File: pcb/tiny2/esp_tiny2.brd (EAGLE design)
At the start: 45 x 95 mm, 35 parts, among them IC1 4000D, Q1 BUZ11BH

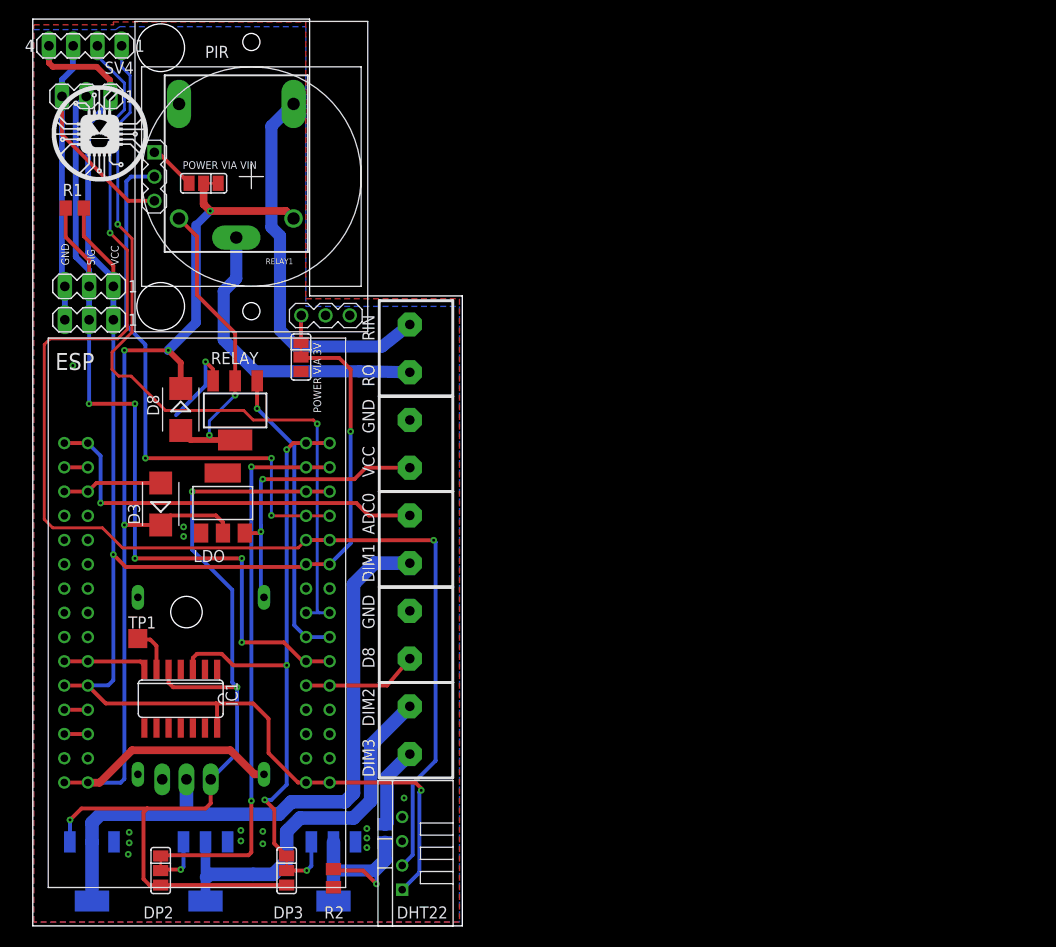
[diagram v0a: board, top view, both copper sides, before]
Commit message: Removed all temp file
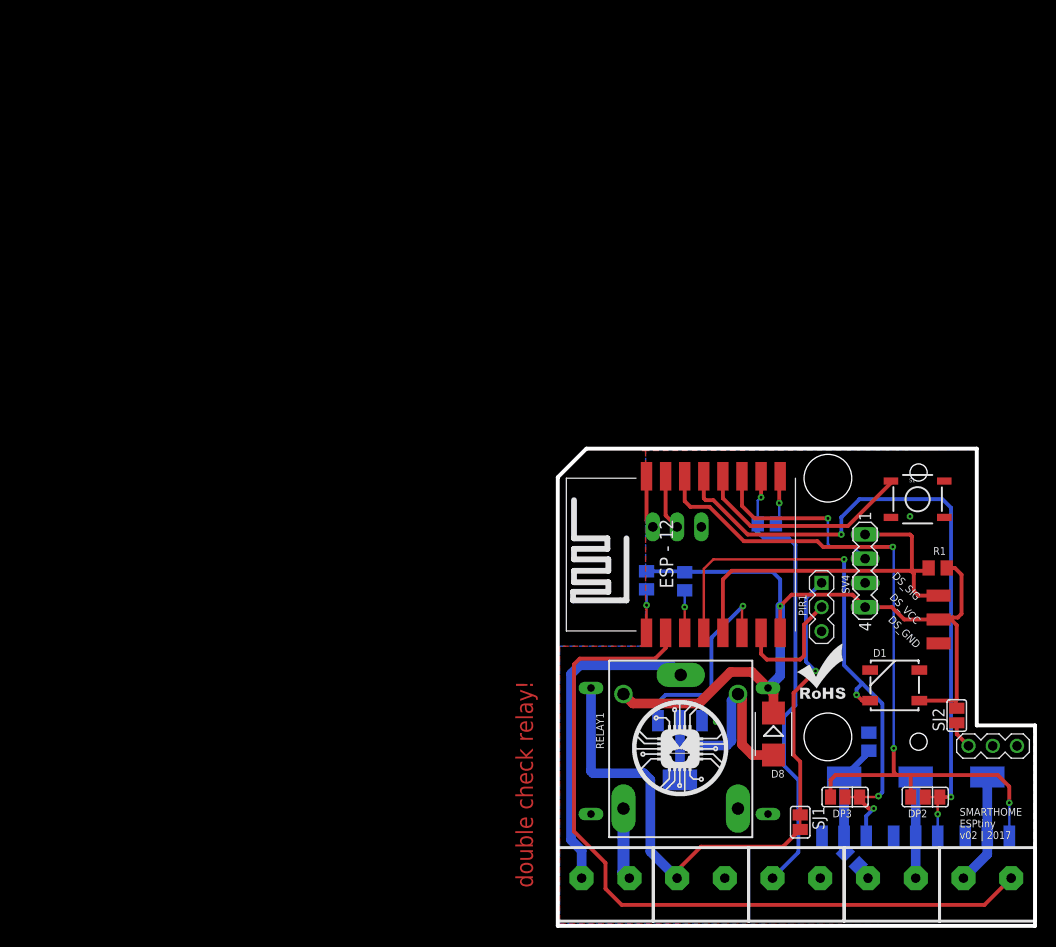
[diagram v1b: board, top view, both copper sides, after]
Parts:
- removed D3: ES2D, diode:SMB
- removed DHT22: TEMP-HUM-SENSOR-DHT22, diy-modules:TEMP-HUM-SENSOR-DHT22
- removed ESP: ESP12E_DEVKIT, ESP12E_DEVKIT:ESP12E_DEVKIT
- removed IC1: 4000D, 40xx:SO14
- removed LDO: REG1117, burr-brown:SOT223
- removed PIR: MOTION-PIR-DYP-ME003, diy-modules:MOTION-PIR-DYP-ME003
- removed Q1: BUZ11BH, transistor-power:TO220BH
- removed SV2, SV3: (no value), con-lstb:MA03-1
- removed TP1: TPTP20SQ, testpad:TP20SQ
- removed U$5, U$6: SMD_SJ_3WAY_CLOSED, JKW_CHIP:SMD_SJ_3WAY_CLOSED
- added D1: (no value), SparkFun-LED:WS2812B
- added DS_GND, DS_SIG, DS_VCC: (no value), wirepad:SMD1,27-2,54
- added PIR1: MOTION-PIR-DYP-ME003, diy-modules:MOTION-PIR-DYP-ME003_FRAMELESS
- added R4, R5, R6: 10k, rcl:M0805
- added S1: TAC_SWITCHSMD, SparkFun-Retired:TACTILE-SWITCH-SMD
- added SJ1: (no value), JKW_CHIP:SMD_SJ_2WAY_CLOSED
- added SJ2: (no value), JKW_CHIP:SMD_SJ_2WAY_OPEN
- added U1: (no value), esp8266modules:ESP12-SMD
- U$12: value MP1584EN_FRAMELESS -> MP1584EN; device JKW_CHIP:MP1584EN_FRAMELESS -> JKW_CHIP:MP1584EN
- moved U$4 104.6 mm to (96.2, 22.7)
- moved SV4 98.5 mm to (87.2, 37.2), turned to 270 degrees
- moved R1 97.9 mm to (94.8, 37.5)
- moved T_DIM1 94.0 mm to (100.0, 12.5), turned to 0 degrees
- moved U$11 88.6 mm to (62.8, 13.6)
- moved U$9 85.8 mm to (79.6, 23.7), flipped to the top
- moved DP2 80.5 mm to (93.5, 13.5), turned to 180 degrees
- moved SV1 76.6 mm to (67.5, 41.8), flipped to the bottom, turned to 0 degrees
- moved RELAY1 76.6 mm to (68.0, 18.9), turned to 270 degrees
- moved T_DIM2 74.7 mm to (92.5, 12.5), turned to 0 degrees
- moved D8 70.8 mm to (77.6, 20.1)
- moved U$3 70.0 mm to (100.0, 4.50), turned to 0 degrees
- moved U$1 61.5 mm to (80.7, 28.9)
- moved U$8 59.5 mm to (60.0, 4.50), turned to 0 degrees
- moved DP3 59.0 mm to (85.1, 13.5), turned to 180 degrees
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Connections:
- removed net DIMM2: DP2.1, ESP.D1, ESP.D11
- removed net N$12: ESP.EN, ESP.EN1
- removed net N$13: ESP.RST, ESP.RST1
- removed net N$14: D3.A, ESP.RSV@1, ESP.RSV@11
- removed net N$17: LDO.3, U$12.VIN, U$7.P$1
- removed net N$24: PIR.4, U$5.1
- removed net N$31: PIR.1, U$6.3
- removed net ONEWIRE_DS12B20: ESP.D7, ESP.D71, R1.1, SV1.2, SV2.2, SV3.2
- removed net RERLAY: ESP.D6, ESP.D61, RELAY.1
- new net 12V_PIR: PIR1.1, SJ1.1
- new net 3.3V_PIR: PIR1.4, SJ2.1
- new net A_IN: U$3.P$2, U1.ADC
- new net N$6: SV1.2, U1.RXD0
- new net N$7: S1.1, U1.GPIO0
- new net N$8: DP2.1, U1.GPIO5
- new net RELAY: RELAY.1, U1.GPIO12
- net DHT_SIG/SDA: now also U1.GPIO2; no longer DHT22.2, ESP.D4, ESP.D41
- net DIMM1: now also U1.GPIO4; no longer ESP.D2, ESP.D21, IC1.5, Q1.G
- net DIMM3: now also D1.4, U1.GPIO16; no longer ESP.D0, ESP.D01, IC1.3
- net DIMMING1: no longer Q1.D
- net EARTH_HUM_POW: now also R5.1, U1.GPIO15; no longer ESP.D8, ESP.D81
- net GND: now also D1.3, DS_GND.1, PIR1.3, R5.2, S1.3, SV1.1, U1.GND; no longer DHT22.4, ESP.GND@0, ESP.GND@1, ESP.GND@2, ESP.GND@3, ESP.GND@4, ESP.GND@5, ESP.GND@6, ESP.GND@7, IC1.7, LDO.1, PIR.3, Q1.S, SV1.3, SV2.3, SV3.3
- net N$1: now also R6.1, U1.CH_PD; no longer ESP.AD0, ESP.AD1, U$3.P$2
- net N$2: now also R4.1, U1.RESET; no longer ESP.RSV@0, ESP.RSV@01
- net N$4: now also SV1.3, U1.TXD0; no longer IC1.6, TP1.TP
- net NORMALLY_OPEN: now also RELAY1.SWOPEN; no longer RELAY1.SWCLOSED
- net PIR: now also PIR1.2, U1.GPIO13; no longer ESP.D3, ESP.D31, PIR.2
- net SCL: now also DS_SIG.1, R1.1, U1.GPIO14; no longer ESP.D5, ESP.D51
- net VCC: now also SJ1.3, U$12.VIN, U$7.P$1; no longer D3.C, D8.C, ESP.VIN, ESP.VIN1, LDO.2, RELAY1.COIL0, U$12.VOUT, U$6.2
- net VDD: now also D1.1, D8.C, DS_VCC.1, R4.2, R6.2, RELAY1.COIL0, SJ2.3, U$12.VOUT, U1.VCC; no longer DHT22.1, ESP.3V3@0, ESP.3V3@1, ESP.3V3@2, ESP.3V3@3, ESP.3V3@4, ESP.3V3@5, IC1.14, SV1.1, SV2.1, SV3.1, U$5.2
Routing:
- net DHT_SIG/SDA: track 138.4 -> 19.9 mm, vias 2 -> 1
- net VDD: track 194.7 -> 90.2 mm, vias 3 -> 1
- net ONEWIRE_DS12B20: track 94.0 -> 0.00 mm, vias 5 -> 0
- net VCC: track 123.5 -> 42.2 mm, vias 4 -> 0
- net A_IN: track 0.00 -> 81.1 mm
- net N$8: track 0.00 -> 64.2 mm, vias 0 -> 2
- net GND: track 64.1 -> 5.33 mm, vias 15 -> 3
- net DIMM2: track 58.3 -> 0.00 mm, vias 2 -> 0
- net DIMMING1: track 69.3 -> 11.6 mm
- net PIR: track 58.3 -> 13.0 mm, vias 3 -> 0
- net SCL: track 82.5 -> 41.3 mm, vias 2 -> 0
- net N$1: track 42.2 -> 4.45 mm
- net EARTH_HUM_POW: track 12.2 -> 47.8 mm, vias 0 -> 1
- net NORMALLY_OPEN: track 40.1 -> 7.55 mm
- net RERLAY: track 31.4 -> 0.00 mm, vias 1 -> 0
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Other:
- board size 45 x 95 mm -> 50 x 50 mm
- board text added: "SMARTHOME ESPtiny v02 | 2017"
- board text added: "double check relay!"
- board text removed: "DIM1"
- board text removed: "DIM2"
- board text removed: "DIM3"
- board text removed: "POWER VIA 3V"
- board text removed: "POWER VIA VIN"
- board text removed: "SIG"
- board text removed: "SMARTHOME ESP MQTT v03 | 2017"
